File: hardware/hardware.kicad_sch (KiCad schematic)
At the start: 132 parts, among them J1 Conn_01x04_Pin, J10 Conn_01x03, J11 AVR-ISP-6, J12 Conn_01x03, J13 Conn_01x03, J14 Conn_01x03, J2 Conn_01x04_Pin, J3 Conn_01x04_Pin, J4 Conn_01x04_Pin, J5 Conn_01x04_Pin, J6 Conn_01x04_Pin, J7 Conn_01x04_Pin, J8 Conn_01x03, J9 Conn_01x02, K1 RAYEX-L90, K2 RAYEX-L90, P1 USB_C_Plug, Q1 Q_NPN, Q2 Q_NPN, U1 DRV8825PWPR, U2 DRV8825PWPR, U3 DRV8825PWPR, U4 DRV8825PWPR, U5 DRV8825PWPR, U6 DRV8825PWPR, U7 DRV8825PWPR, U8 ATmega2560-16A, U9 CH340C, Y1 Crystal_GND24

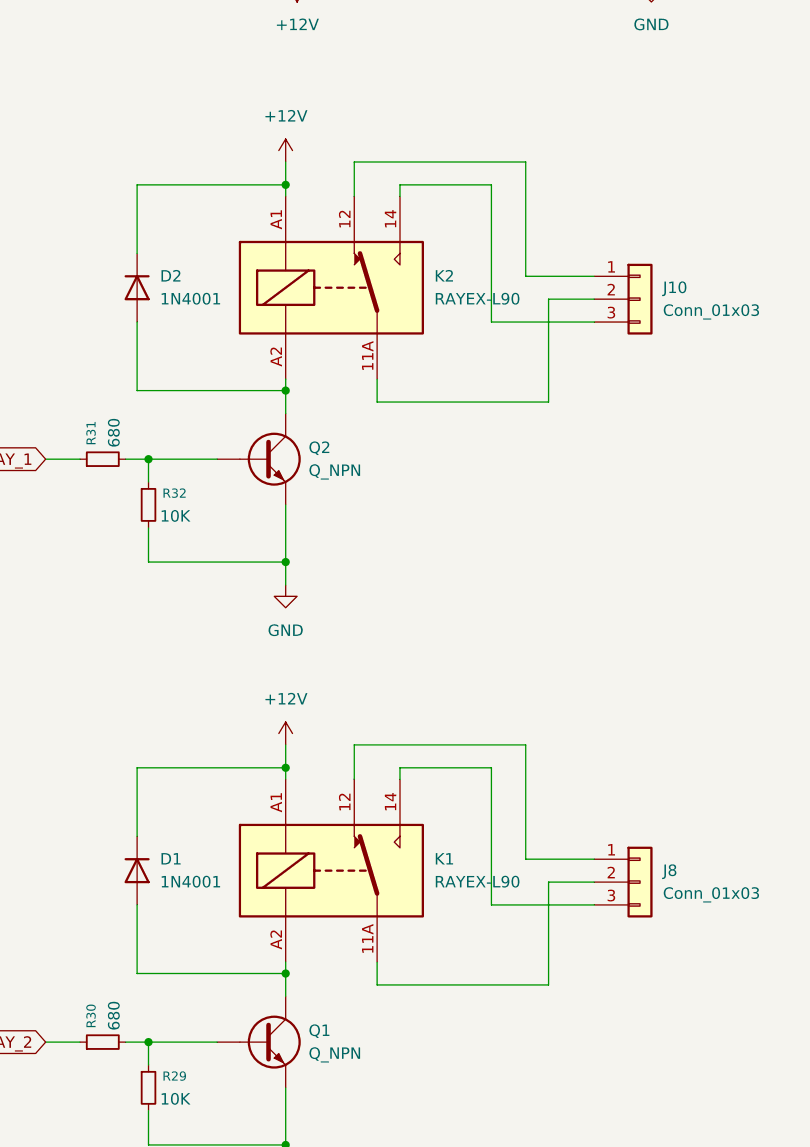
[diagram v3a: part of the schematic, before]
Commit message: placing relay + drv + edit relay footprints
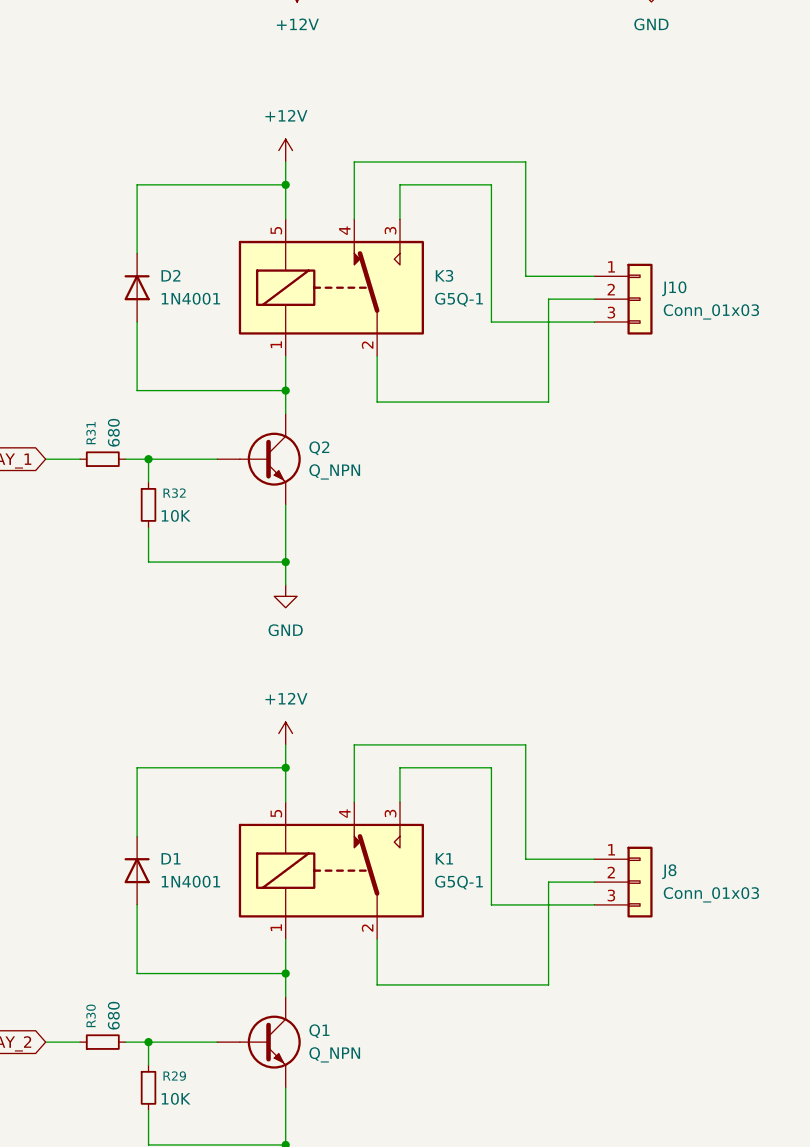
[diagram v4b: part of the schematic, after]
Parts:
- removed K1, K2: RAYEX-L90, Relay_THT:Relay_SPDT_Omron-G5LE-1, symbol Relay:RAYEX-L90
- added K1, K3: G5Q-1, Relay_THT:Relay_SPDT_Omron-G5Q-1, symbol Relay:G5Q-1
- J10, J8: footprint TerminalBlock_Phoenix:TerminalBlock_Phoenix_MPT-0,5-3-2.54_1x03_P2.54mm_Horizontal -> TerminalBlock_TE-Connectivity:TerminalBlock_TE_282834-3_1x03_P2.54mm_Horizontal
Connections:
- net +12V: now also K1.5, K3.5
- net at D2.2 (A), Q2.C: now also K3.1
- net at J8.2 (Pin_2): now also K1.2
- net at J8.1 (Pin_1): now also K1.4
- net at J8.3 (Pin_3): now also K1.3
- net at D1.2 (A), Q1.C: now also K1.1
- net at J10.2 (Pin_2): now also K3.2
- net at J10.1 (Pin_1): now also K3.4
- net at J10.3 (Pin_3): now also K3.3

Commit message: wire all drv
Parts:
- removed R11, R19, R20, R21, R27, R3, R7: 1M, Resistor_SMD:R_0603_1608Metric, symbol Device:R_Small
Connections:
- removed net +3.3V: C11.2, C19.2, C20.2, C21.2, C27.2, C3.2, C7.2, RV1.1, RV2.1, RV3.1, RV4.1, RV5.1, RV6.1, RV7.1, U1.15 (V3P3OUT), U2.15 (V3P3OUT), U3.15 (V3P3OUT), U4.15 (V3P3OUT), U5.15 (V3P3OUT), U6.15 (V3P3OUT), U7.15 (V3P3OUT)
- new net 3.3_1: C3.2, RV1.1, U1.15 (V3P3OUT)
- new net 3.3_2: C7.2, RV2.1, U2.15 (V3P3OUT)
- new net 3.3_3: C11.2, RV3.1, U3.15 (V3P3OUT)
- new net 3.3_4: C19.2, RV4.1, U4.15 (V3P3OUT)
- new net 3.3_5: C20.2, RV5.1, U5.15 (V3P3OUT)
- new net 3.3_6: C21.2, RV6.1, U6.15 (V3P3OUT)
- new net 3.3_7: C27.2, RV7.1, U7.15 (V3P3OUT)

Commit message: finish pcb wiring
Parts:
- removed Q1, Q2: Q_NPN, Package_TO_SOT_SMD:TSOT-23_HandSoldering, symbol Device:Q_NPN
- added C38, C39: 10u, Capacitor_SMD:C_0603_1608Metric, symbol Device:C
- added C40: 0.1µF, Capacitor_SMD:C_0603_1608Metric, symbol Device:C
- added C41, C42: 22u, Capacitor_SMD:C_0603_1608Metric, symbol Device:C
- added L2: 4.7uH, Inductor_SMD:L_Chilisin_BMRA00050520, symbol Device:L
- added Q1, Q2: AO3400A, Package_TO_SOT_SMD:SOT-23, symbol Transistor_FET:AO3400A
- added R3: 10K, Resistor_SMD:R_0603_1608Metric, symbol Device:R_Small
- added R7: 33.0K, Resistor_SMD:R_0603_1608Metric, symbol Device:R_Small
- added U10: TPS562200, Package_TO_SOT_SMD:SOT-23-6, symbol Regulator_Switching:TPS562200
- J12, J13, J14: footprint (none) -> Connector_PinHeader_2.54mm:PinHeader_1x03_P2.54mm_Vertical
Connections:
- net +12V: now also C38.1, C39.1, U10.3 (VIN), U10.5 (EN)
- net GND: now also C38.2, C39.2, C41.2, C42.2, Q1.2 (S), Q2.2 (S), R3.2, U10.1 (GND)
- net SERVO_1: now also U8.7 (PE5)
- net SERVO_2: now also U8.6 (PE4)
- net SERVO_3: now also U8.5 (PE3)
- net at R31.2, R32.1: now also Q2.1 (G)
- net at D2.2 (A), K3.1: now also Q2.3 (D)
- net at R29.1, R30.2: now also Q1.1 (G)
- net at D1.2 (A), K1.1: now also Q1.3 (D)
- net at J10.1 (Pin_1): now also K3.3; no longer K3.4
- net at J10.3 (Pin_3): now also K3.4; no longer K3.3
- net at K1.3: now also J8.1 (Pin_1); no longer J8.3 (Pin_3)
- net at K1.4: now also J8.3 (Pin_3); no longer J8.1 (Pin_1)
- net STEP_7: now reaches U8.36 (PL1)
- net STEP_7: now also U7.22 (STEP)
- net DIR_7: now reaches U8.37 (PL2)
- net DIR_7: now also U7.20 (DIR)
- net STEP_6: now reaches U8.38 (PL3)
- net STEP_6: now also U6.22 (STEP)
- net DIR_6: now reaches U8.39 (PL4)
- net DIR_6: now also U6.20 (DIR)
- net STEP_5: now reaches U8.40 (PL5)
- net STEP_5: now also U5.22 (STEP)
- net DIR_5: now reaches U8.41 (PL6)
- net DIR_5: now also U5.20 (DIR)
- net SCL: now reaches U8.43 (PD0)
- net SDA: now reaches U8.44 (PD1)
- net RX1: now reaches U8.45 (PD2)
- net TX1: now reaches U8.46 (PD3)
- net STEP_4: now reaches U8.53 (PC0)
- net STEP_4: now also U4.22 (STEP)
- net DIR_4: now reaches U8.54 (PC1)
- net DIR_4: now also U4.20 (DIR)
- net STEP_3: now reaches U8.55 (PC2)
- net STEP_3: now also U3.22 (STEP)
- net DIR_3: now reaches U8.56 (PC3)
- net DIR_3: now also U3.20 (DIR)
- net STEP_2: now reaches U8.57 (PC4)
- net STEP_2: now also U2.22 (STEP)
- net DIR_2: now reaches U8.58 (PC5)
- net DIR_2: now also U2.20 (DIR)
- net STEP_1: now reaches U8.59 (PC6)
- net STEP_1: now also U1.22 (STEP)
- net DIR_1: now reaches U8.60 (PC7)
- net DIR_1: now also U1.20 (DIR)
- removed net DIR: U1.20 (DIR), U2.20 (DIR), U3.20 (DIR), U4.20 (DIR), U5.20 (DIR), U6.20 (DIR), U7.20 (DIR)
- removed net STEP: U1.22 (STEP), U2.22 (STEP), U3.22 (STEP), U4.22 (STEP), U5.22 (STEP), U6.22 (STEP), U7.22 (STEP)
- net VBUS renamed +5V
- net +5V: now also C41.1, C42.1, L2.2, R7.2
- new net: C40.2, L2.1, U10.2 (SW)
- new net: R3.1, R7.1, U10.4 (VFB)
- new net: C40.1, U10.6 (VBST)

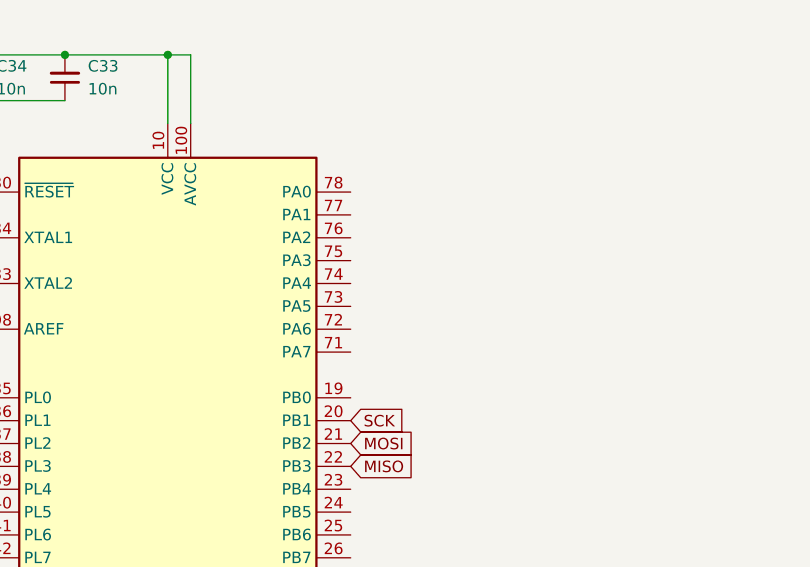
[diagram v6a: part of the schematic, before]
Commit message: fix relay +led wiring
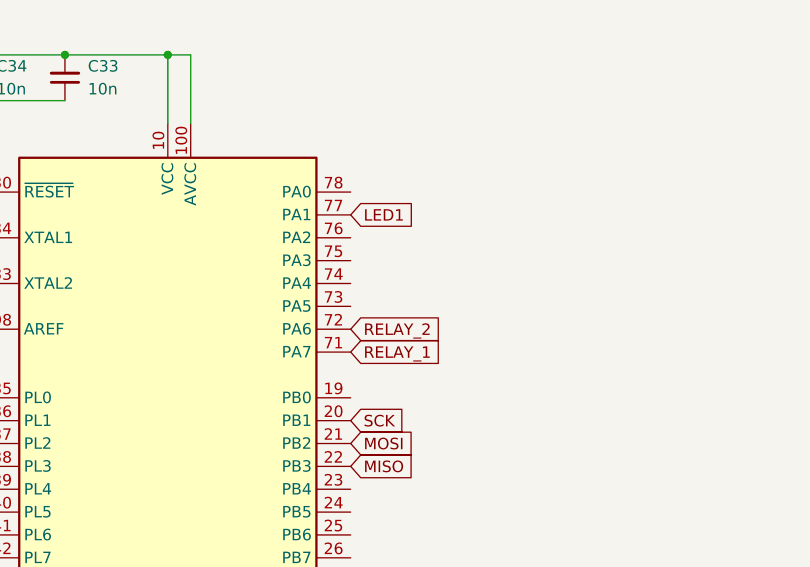
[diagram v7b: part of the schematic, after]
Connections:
- net LED1: now also U8.77 (PA1)
- net RELAY_1: now also U8.71 (PA7)
- net RELAY_2: now also U8.72 (PA6)
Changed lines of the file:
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@@
+		)
+	)
+	(global_label "LED1"
+		(shape input)
+		(at 219.71 132.08 0)
+		(fields_autoplaced yes)
+		(effects
+			(font
+				(size 1.27 1.27)
+			)
+			(justify left)
+		)
+		(property "Intersheetrefs" "${INTERSHEET_REFS}"
+			(at 227.3518 132.08 0)
+			(effects
+				(font
+					(size 1.27 1.27)
+				)
+				(justify left)
+				(hide yes)
+			)
 		)
 	)
@@
 		)
 	)
+	(global_label "RELAY_1"
+		(shape input)
+		(at 219.71 147.32 0)
+		(fields_autoplaced yes)
+		(effects
+			(font
+				(size 1.27 1.27)
+			)
+			(justify left)
+		)
+		(property "Intersheetrefs" "${INTERSHEET_REFS}"
+			(at 230.4966 147.32 0)
+			(effects
+				(font
+					(size 1.27 1.27)
+				)
+				(justify left)
+				(hide yes)
+			)
+		)
+	)
 	(global_label "SCK"
 		(shape input)
@@
 			(effects
 				(font
+					(size 1.27 1.27)
+				)
+				(justify left)
+				(hide yes)
+			)
+		)
+	)
+	(global_label "RELAY_2"
+		(shape input)
+		(at 219.71 144.78 0)
+		(fields_autoplaced yes)
+		(effects
+			(font
+				(size 1.27 1.27)
+			)
+			(justify left)
+		)
+		(property "Intersheetrefs" "${INTERSHEET_REFS}"
+			(at 230.4966 144.78 0)
+			(effects
+				(font

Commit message: wire current regulator
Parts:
- added C43, C44, C45: 100n, Capacitor_SMD:CP_Elec_6.3x5.7, symbol Device:C_Polarized
- added C46: 10pf, Capacitor_SMD:C_0603_1608Metric, symbol Device:C_Small
- added D5: LED, LED_SMD:LED_0603_1608Metric, symbol Device:LED
- added J15: Conn_02x05_Odd_Even, Connector_PinHeader_2.54mm:PinHeader_2x05_P2.54mm_Vertical, symbol Connector_Generic:Conn_02x05_Odd_Even
- added J16: Conn_01x02, Connector_Molex:Molex_KK-254_AE-6410-02A_1x02_P2.54mm_Vertical, symbol Connector_Generic:Conn_01x02
- added R11, R19, R20, R21, R27: 10K, Resistor_SMD:R_0603_1608Metric, symbol Device:R_Small
- added R35: 1.1K, Resistor_SMD:R_0603_1608Metric, symbol Device:R_Small
- added R36: 12, Resistor_SMD:R_1206_3216Metric, symbol Device:R_Small
- added U11: LM317_SOT-223, Package_TO_SOT_SMD:SOT-223-3_TabPin2, symbol Regulator_Linear:LM317_SOT-223
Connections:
- net +12V: now also C43.1, C44.1, C45.1, C46.1, U11.3 (VI)
- net +5V: now also R11.2, R19.2, R20.2, R21.2, R27.2
- net GND: now also C43.2, C44.2, C45.2, C46.2, D5.1 (K), J15.1 (Pin_1), J15.3 (Pin_3), J15.5 (Pin_5), J15.7 (Pin_7), J15.9 (Pin_9), J16.2 (Pin_2)
- net RX: now also U8.2 (PE0); no longer U8.3 (PE1)
- net TX: now also U8.3 (PE1); no longer U8.2 (PE0)
- net END_STOP_1: now reaches U8.63 (PJ0)
- net END_STOP_1: now also J15.10 (Pin_10), R11.1
- net END_STOP_2: now reaches U8.64 (PJ1)
- net END_STOP_2: now also J15.8 (Pin_8), R19.1
- net END_STOP_3: now reaches U8.65 (PJ2)
- net END_STOP_3: now also J15.6 (Pin_6), R20.1
- net END_STOP_4: now reaches U8.66 (PJ3)
- net END_STOP_4: now also J15.4 (Pin_4), R21.1
- net END_STOP_5: now reaches U8.67 (PJ4)
- net END_STOP_5: now also J15.2 (Pin_2), R27.1
- net LED2: now reaches U8.78 (PA0)
- net LED2: now also R35.1
- new net: J16.1 (Pin_1), R36.2, U11.1 (ADJ)
- new net: D5.2 (A), R35.2
- new net: R36.1, U11.2 (VO)
